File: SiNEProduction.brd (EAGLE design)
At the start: 80 x 60 mm, 35 parts, among them IC1 74HCT164D, IC3 ATTINY24/44/84-SSU, J1 AVR_SPI_PRG_6NS

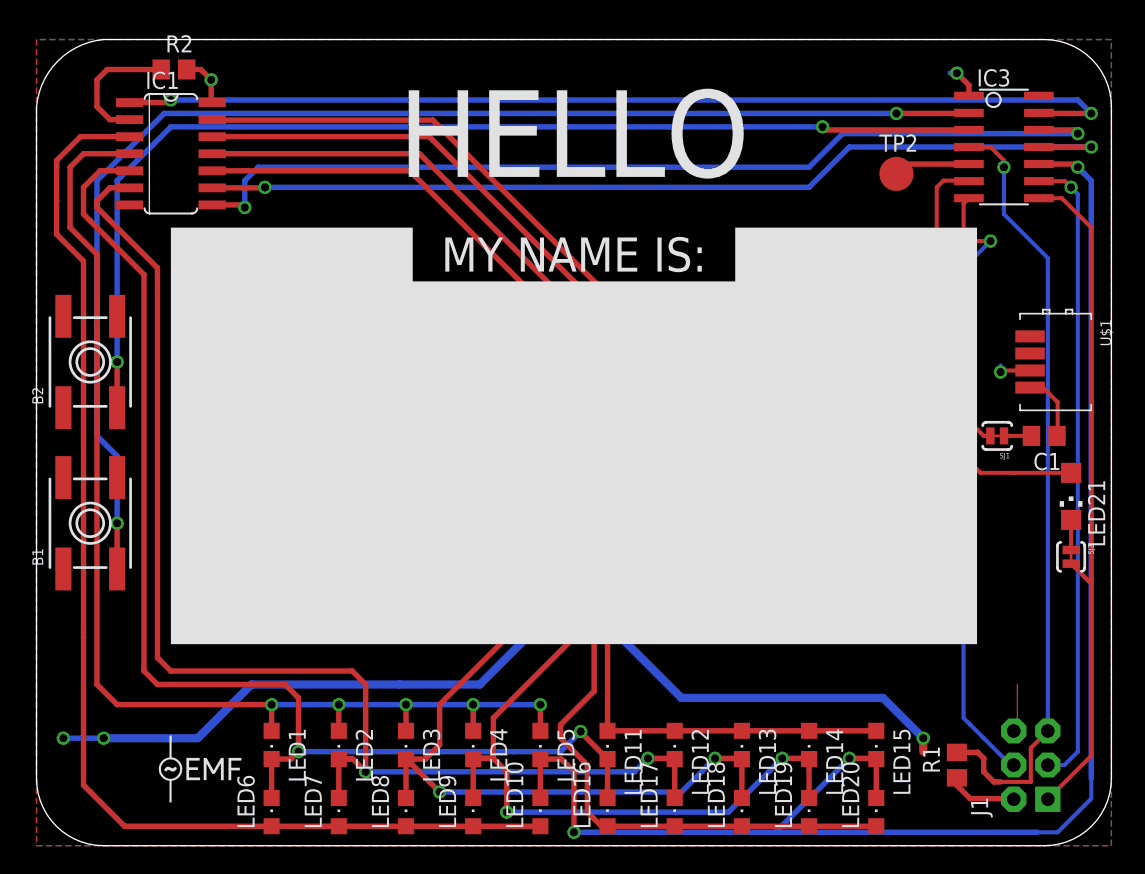
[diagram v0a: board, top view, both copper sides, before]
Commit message: Moved Battery clip up a little, added bRestrict for better contact Fixed trace width in lower right corner
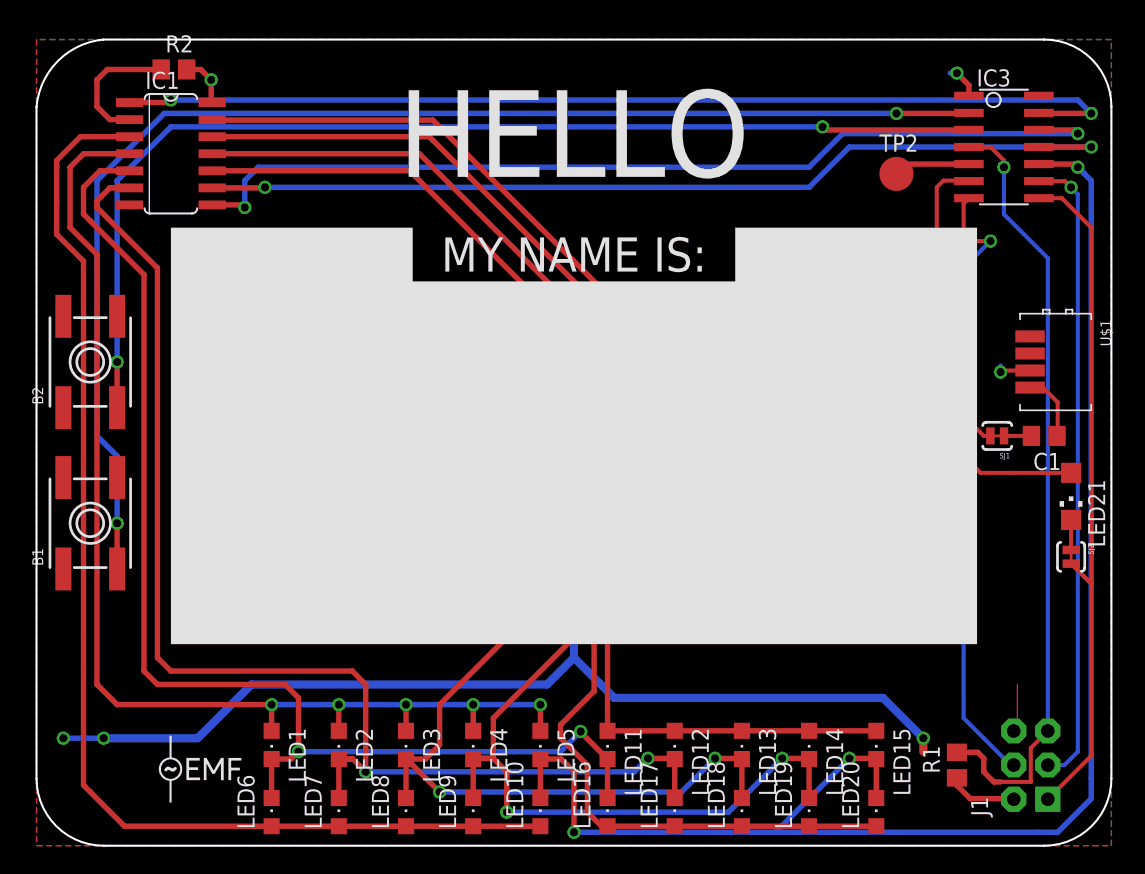
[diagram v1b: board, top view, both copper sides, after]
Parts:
- moved BAT2 3.00 mm to (40.0, 22.0)
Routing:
- net GND: track 77.7 -> 81.5 mm
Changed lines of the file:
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@@
 <layer number="44" name="Drills" color="7" fill="1" visible="no" active="yes"/>
 <layer number="45" name="Holes" color="7" fill="1" visible="no" active="yes"/>
-<layer number="46" name="Milling" color="3" fill="1" visible="no" active="yes"/>
+<layer number="46" name="Milling" color="3" fill="1" visible="yes" active="yes"/>
 <layer number="47" name="Measures" color="7" fill="1" visible="no" active="yes"/>
 <layer number="48" name="Document" color="7" fill="1" visible="yes" active="yes"/>
-<layer number="49" name="Reference" color="7" fill="1" visible="yes" active="yes"/>
+<layer number="49" name="Reference" color="13" fill="1" visible="yes" active="yes"/>
 <layer number="50" name="dxf" color="7" fill="1" visible="no" active="no"/>
-<layer number="51" name="tDocu" color="7" fill="1" visible="yes" active="yes"/>
+<layer number="51" name="tDocu" color="14" fill="1" visible="no" active="yes"/>
 <layer number="52" name="bDocu" color="7" fill="1" visible="no" active="yes"/>
 <layer number="53" name="tGND_GNDA" color="7" fill="9" visible="no" active="no"/>
@@
 <board>
 <plain>
-<wire x1="0" y1="5" x2="0" y2="55" width="0" layer="20"/>
-<wire x1="5" y1="60" x2="75" y2="60" width="0" layer="20"/>
-<wire x1="80" y1="55" x2="80" y2="5" width="0" layer="20"/>
-<wire x1="75" y1="0" x2="5" y2="0" width="0" layer="20"/>
-<wire x1="0" y1="5" x2="5" y2="0" width="0" layer="20" curve="90"/>
-<wire x1="75" y1="0" x2="80" y2="5" width="0" layer="20" curve="90"/>
-<wire x1="75" y1="60" x2="80" y2="55" width="0" layer="20" curve="-90"/>
-<wire x1="5" y1="60" x2="0" y2="55" width="0" layer="20" curve="79.611142"/>
+<wire x1="0" y1="5" x2="0" y2="55" width="0.15" layer="20"/>
+<wire x1="5" y1="60" x2="75" y2="60" width="0.15" layer="20"/>
+<wire x1="80" y1="55" x2="80" y2="5" width="0.15" layer="20"/>
+<wire x1="75" y1="0" x2="5" y2="0" width="0.15" layer="20"/>
+<wire x1="0" y1="5" x2="5" y2="0" width="0.15" layer="20" curve="90"/>
+<wire x1="75" y1="0" x2="80" y2="5" width="0.15" layer="20" curve="90"/>
+<wire x1="75" y1="60" x2="80" y2="55" width="0.15" layer="20" curve="-90"/>
+<wire x1="5" y1="60" x2="0" y2="55" width="0.15" layer="20" curve="79.611142"/>
 <text x="40" y="53" size="6.4516" layer="21" align="center">HELLO</text>
 <polygon width="0" layer="21">
@@
 </polygon>
 <text x="40" y="44" size="2.54" layer="21" align="center">MY NAME IS:</text>
+<circle x="40" y="22" radius="9" width="0" layer="42"/>
 </plain>
 <attributes>
@@
 <param name="layerSetup" value="(1*16)"/>
 <param name="mtCopper" value="0.035mm 0.035mm 0.035mm 0.035mm 0.035mm 0.035mm 0.035mm 0.035mm 0.035mm 0.035mm 0.035mm 0.035mm 0.035mm 0.035mm 0.035mm 0.035mm"/>
-<param name="mtIsolate" value="1.5mm 0.15mm 0.2mm 0.15mm 0.2mm 0.15mm 0.2mm 0.15mm 0.2mm 0.15mm 0.2mm 0.15mm 0.2mm 0.15mm 0.2mm"/>
-<param name="mdWireWire" value="8mil"/>
-<param name="mdWirePad" value="8mil"/>
-<param name="mdWireVia" value="8mil"/>
-<param name="mdPadPad" value="8mil"/>
-<param name="mdPadVia" value="8mil"/>
-<param name="mdViaVia" value="8mil"/>
-<param name="mdSmdPad" value="8mil"/>
-<param name="mdSmdVia" value="8mil"/>
-<param name="mdSmdSmd" value="8mil"/>
+<param name="mtIsolate" value="1mm 0.15mm 0.2mm 0.15mm 0.2mm 0.15mm 0.2mm 0.15mm 0.2mm 0.15mm 0.2mm 0.15mm 0.2mm 0.15mm 0.2mm"/>
+<param name="mdWireWire" value="0.15mm"/>
+<param name="mdWirePad" value="0.15mm"/>
+<param name="mdWireVia" value="0.15mm"/>
+<param name="mdPadPad" value="0.15mm"/>
+<param name="mdPadVia" value="0.15mm"/>
+<param name="mdViaVia" value="0.15mm"/>
+<param name="mdSmdPad" value="0mil"/>
+<param name="mdSmdVia" value="0mil"/>
+<param name="mdSmdSmd" value="0mil"/>
 <param name="mdViaViaSameLayer" value="8mil"/>
 <param name="mnLayersViaInSmd" value="2"/>
-<param name="mdCopperDimension" value="40mil"/>
-<param name="mdDrill" value="8mil"/>
+<param name="mdCopperDimension" value="0.15mm"/>
+<param name="mdDrill" value="0.15mm"/>
 <param name="mdSmdStop" value="0mil"/>
-<param name="msWidth" value="10mil"/>
-<param name="msDrill" value="24mil"/>
-<param name="msMicroVia" value="9.99mm"/>
+<param name="msWidth" value="0.15mm"/>
+<param name="msDrill" value="0.3mm"/>
+<param name="msMicroVia" value="0.3mm"/>
 <param name="msBlindViaRatio" value="0.5"/>
 <param name="rvPadTop" value="0.25"/>
@@
 <param name="mlMinCreamFrame" value="0mil"/>
 <param name="mlMaxCreamFrame" value="0mil"/>
-<param name="mlViaStopLimit" value="0mil"/>
+<param name="mlViaStopLimit" value="23mil"/>
 <param name="srRoundness" value="0"/>
 <param name="srMinRoundness" value="0mil"/>
@@
 <element name="U$1" library="SiNE Parts" package="TSOP35X" value="IR-RECEIVER" x="76" y="36" rot="R270"/>
 <element name="IC3" library="SiNE Parts" package="SOIC14" value="ATTINY24/44/84-SSU" x="72" y="52" rot="R270"/>
-<element name="BAT2" library="SiNE Parts" package="BATTCON_20MM" value="" x="40" y="19" rot="MR0"/>
+<element name="BAT2" library="SiNE Parts" package="BATTCON_20MM" value="" x="40" y="22" rot="MR0"/>
 <element name="TP2" library="SiNE Parts" package="B2,54" value="TPB2,54" x="64" y="50">
 <attribute name="TP_SIGNAL_NAME" value="" x="79.24" y="-21.12" size="1.778" layer="27" display="off"/>
@@
 <contactref element="B2" pad="B'"/>
 <contactref element="B1" pad="B'"/>
-<wire x1="40" y1="19" x2="33" y2="12" width="0.6096" layer="16"/>
-<wire x1="33" y1="12" x2="27" y2="12" width="0.6096" layer="16"/>
-<wire x1="27" y1="12" x2="16" y2="12" width="0.6096" layer="16"/>
+<wire x1="40" y1="14" x2="38" y2="12" width="0.6096" layer="16"/>
+<wire x1="38" y1="12" x2="16" y2="12" width="0.6096" layer="16"/>
 <wire x1="16" y1="12" x2="12" y2="8" width="0.6096" layer="16"/>
 <wire x1="12" y1="8" x2="5" y2="8" width="0.6096" layer="16"/>
-<wire x1="40" y1="19" x2="48" y2="11" width="0.6096" layer="16"/>
-<wire x1="48" y1="11" x2="63" y2="11" width="0.6096" layer="16"/>
+<wire x1="40" y1="22" x2="40" y2="14" width="0.6096" layer="16"/>
+<wire x1="40" y1="14" x2="43" y2="11" width="0.6096" layer="16"/>
+<wire x1="43" y1="11" x2="63" y2="11" width="0.6096" layer="16"/>
 <wire x1="63" y1="11" x2="66" y2="8" width="0.6096" layer="16"/>
 <via x="66" y="8" extent="1-16" drill="0.6"/>
@@
 <via x="77.5" y="50.5" extent="1-16" drill="0.6"/>
 <wire x1="77.5" y1="50.5" x2="78" y2="50" width="0.4064" layer="16"/>
-<wire x1="74.5" y1="1" x2="76" y2="1" width="0.3048" layer="16"/>
-<wire x1="76" y1="1" x2="78" y2="3" width="0.3048" layer="16"/>
-<wire x1="78.5" y1="5" x2="78.5" y2="3.5" width="0.3048" layer="16"/>
-<wire x1="78.5" y1="3.5" x2="78" y2="3" width="0.3048" layer="16"/>
+<wire x1="74.5" y1="1" x2="76" y2="1" width="0.4064" layer="16"/>
+<wire x1="76" y1="1" x2="78" y2="3" width="0.4064" layer="16"/>
+<wire x1="78.5" y1="5" x2="78.5" y2="3.5" width="0.4064" layer="16"/>
+<wire x1="78.5" y1="3.5" x2="78" y2="3" width="0.4064" layer="16"/>
 </signal>
 <signal name="LED_R1">

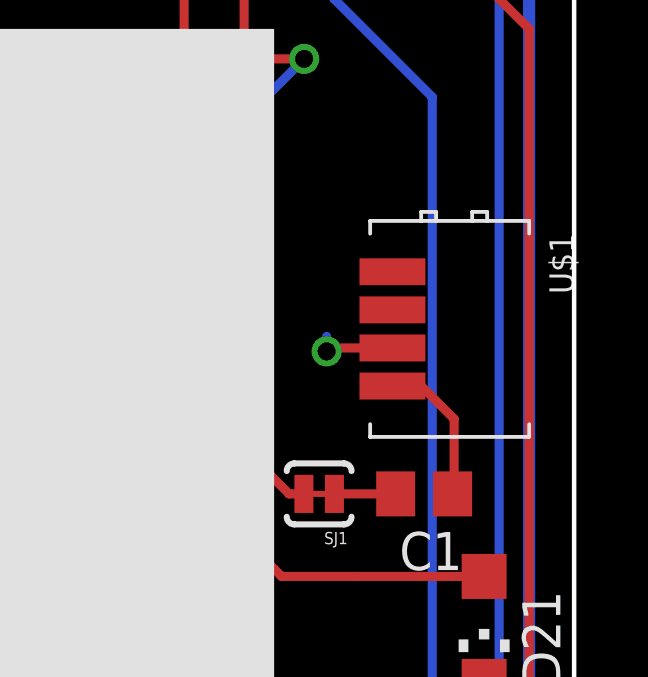
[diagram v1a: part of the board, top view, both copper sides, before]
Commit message: Updated to use the combined IR Receiver footprint in case we have to switch parts
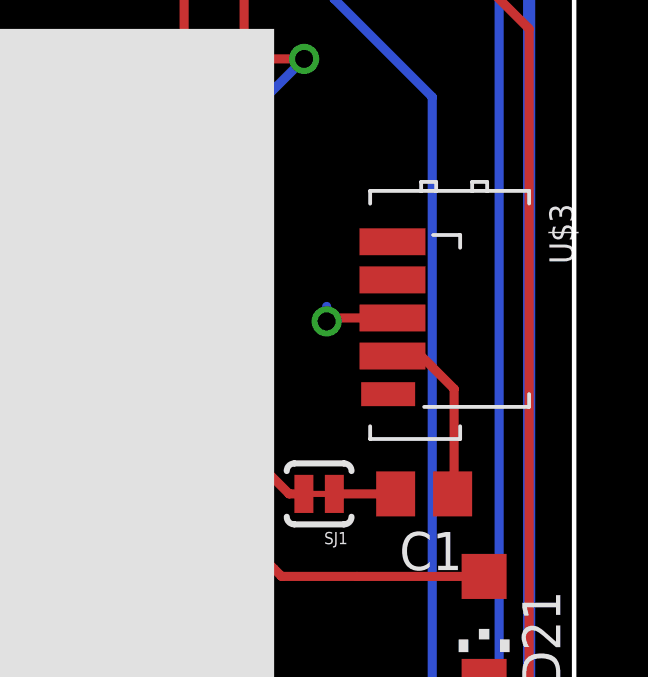
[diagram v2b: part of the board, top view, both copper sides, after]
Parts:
- removed U$1: IR-RECEIVER, SiNE Parts:TSOP35X
- added U$3: IR-RECEIVE-COMBINED, SiNE Parts:TSOP-COMBINED
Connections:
- net GND: now also U$3.1, U$3.2, U$3.5; no longer U$1.1, U$1.2
- net N$6: now also U$3.4; no longer U$1.4
- net VCC: now also U$3.3; no longer U$1.3
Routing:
- net N$6: track 5.09 -> 6.09 mm
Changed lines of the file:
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@@
 <element name="SJ1" library="SparkFun" package="SJ_2S-TRACE" value="SOLDERJUMPERTRACE (NP)" x="71.5" y="30.5" rot="R180"/>
 <element name="SJ2" library="SparkFun" package="SJ_2S-TRACE" value="SOLDERJUMPERTRACE (NP)" x="77" y="21.5" rot="R270"/>
-<element name="U$1" library="SiNE Parts" package="TSOP35X" value="IR-RECEIVER" x="76" y="36" rot="R270"/>
 <element name="IC3" library="SiNE Parts" package="SOIC14" value="ATTINY24/44/84-SSU" x="72" y="52" rot="R270"/>
 <element name="BAT2" library="SiNE Parts" package="BATTCON_20MM" value="" x="40" y="22" rot="MR0"/>
@@
 <element name="IC1" library="SiNE Parts" package="SO14" value="74HCT164D" x="10" y="51.5" rot="R270"/>
 <element name="U$2" library="TiLDA" package="EMF-SMALL" value="MINIEMF" x="9" y="3"/>
+<element name="U$3" library="SiNE Parts" package="TSOP-COMBINED" value="IR-RECEIVE-COMBINED" x="76" y="37" rot="R270"/>
 </elements>
 <signals>
@@
 <contactref element="B2" pad="B"/>
 <contactref element="B1" pad="B"/>
-<contactref element="U$1" pad="1"/>
-<contactref element="U$1" pad="2"/>
 <polygon width="0.4064" layer="1">
 <vertex x="0" y="0"/>
@@
 <wire x1="72.73" y1="8.54" x2="73" y2="8.81" width="0" layer="1"/>
 <wire x1="73" y1="8.81" x2="73" y2="12" width="0" layer="1"/>
+<contactref element="U$3" pad="1"/>
+<contactref element="U$3" pad="2"/>
+<contactref element="U$3" pad="5"/>
 </signal>
 <signal name="VCC">
@@
 <contactref element="R1" pad="1"/>
 <contactref element="R2" pad="2"/>
-<contactref element="U$1" pad="3"/>
 <polygon width="0.4064" layer="16">
 <vertex x="0" y="0"/>
@@
 <wire x1="69.5" y1="3.5" x2="72.69" y2="3.5" width="0.4064" layer="1"/>
 <wire x1="72.69" y1="3.5" x2="72.73" y2="3.46" width="0.4064" layer="1"/>
-<wire x1="73.945" y1="35.365" x2="71.865" y2="35.365" width="0.3048" layer="1"/>
-<wire x1="71.865" y1="35.365" x2="71.75" y2="35.25" width="0.3048" layer="1"/>
-<via x="71.75" y="35.25" extent="1-16" drill="0.6"/>
-<wire x1="71.75" y1="35.25" x2="71.75" y2="35.75" width="0.3048" layer="16"/>
+<wire x1="73.945" y1="36.365" x2="71.865" y2="36.365" width="0.3048" layer="1"/>
+<wire x1="71.865" y1="36.365" x2="71.75" y2="36.25" width="0.3048" layer="1"/>
+<via x="71.75" y="36.25" extent="1-16" drill="0.6"/>
+<wire x1="71.75" y1="36.25" x2="71.75" y2="36.75" width="0.3048" layer="16"/>
+<contactref element="U$3" pad="3"/>
 </signal>
 <signal name="MOSI">
@@
 <signal name="N$6">
 <contactref element="C1" pad="1"/>
-<contactref element="U$1" pad="4"/>
-<wire x1="73.9" y1="34.05" x2="73.945" y2="34.095" width="0.3048" layer="1"/>
-<wire x1="73.945" y1="34.095" x2="74.905" y2="34.095" width="0.3048" layer="1"/>
-<wire x1="74.905" y1="34.095" x2="76" y2="33" width="0.3048" layer="1"/>
-<wire x1="76" y1="33" x2="76" y2="30.55" width="0.3048" layer="1"/>
+<wire x1="73.9" y1="35.05" x2="73.945" y2="35.095" width="0.3048" layer="1"/>
+<wire x1="73.945" y1="35.095" x2="74.905" y2="35.095" width="0.3048" layer="1"/>
+<wire x1="74.905" y1="35.095" x2="76" y2="34" width="0.3048" layer="1"/>
+<wire x1="76" y1="34" x2="76" y2="30.55" width="0.3048" layer="1"/>
 <wire x1="76" y1="30.55" x2="75.95" y2="30.5" width="0.3048" layer="1"/>
+<contactref element="U$3" pad="4"/>
 </signal>
 <signal name="IR_IN">
